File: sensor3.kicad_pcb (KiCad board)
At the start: 2 copper layers, 25 x 70 mm, 21 parts, among them CON1 AVR-ISP-6, CON2 DM3AT-SF-PEJM5, IC1 ATMEGA328P-A, P1 POWER, P2 RX/TX, P3 I2C, SW1 START/STOP, SW2 FORMAT, U1 AE-LPS331AP, U2 SL-MPU9150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

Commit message: Modify for halfside
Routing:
- net N-0000040: track 24.4 -> 23.7 mm
- net N-0000041: track 25.8 -> 26.4 mm
- net N-0000010: track 22.5 -> 22.8 mm, vias 4 -> 2
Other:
- net class Bold: via_dia 0.889 -> 1.27
- net class Default: trace_width 0.2032 -> 0.254; via_dia 0.889 -> 1.27

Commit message: Up via width
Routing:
- net GND: track 211.8 -> 211.0 mm
- net N-0000010: track 22.8 -> 23.4 mm
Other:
- net class Bold: via_dia 1.27 -> 1.397
- net class Default: via_dia 1.27 -> 1.397

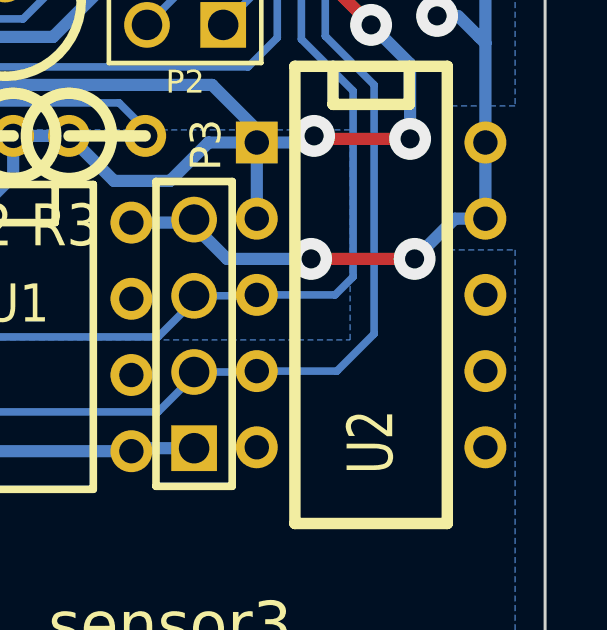
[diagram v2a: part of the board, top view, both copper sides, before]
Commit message: Connect FSYNC to GND
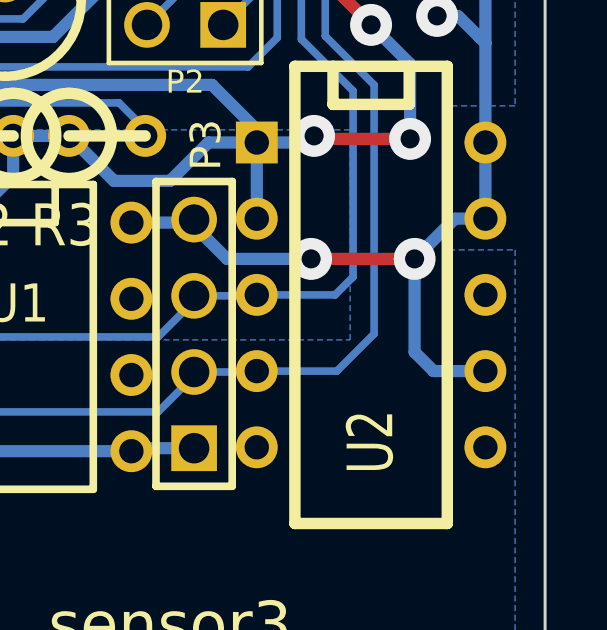
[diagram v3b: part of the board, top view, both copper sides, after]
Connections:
- U2 pad 7: (no net) -> GND
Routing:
- net GND: track 211.0 -> 216.7 mm
